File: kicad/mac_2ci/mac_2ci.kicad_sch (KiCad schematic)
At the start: 17 parts, among them U2 74HC00, U3 74HC00

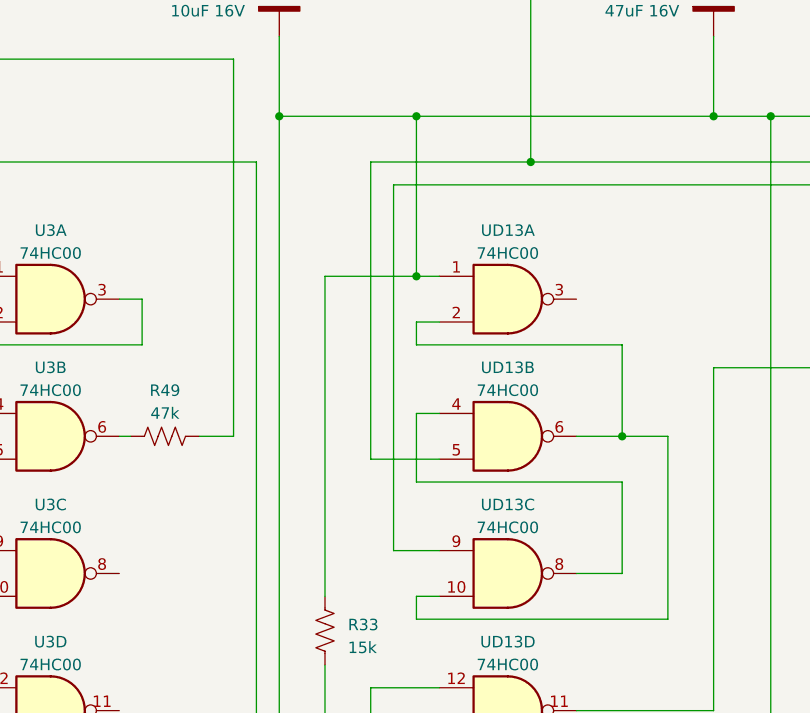
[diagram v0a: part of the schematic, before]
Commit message: Fix connections between UB-13 and UD-13
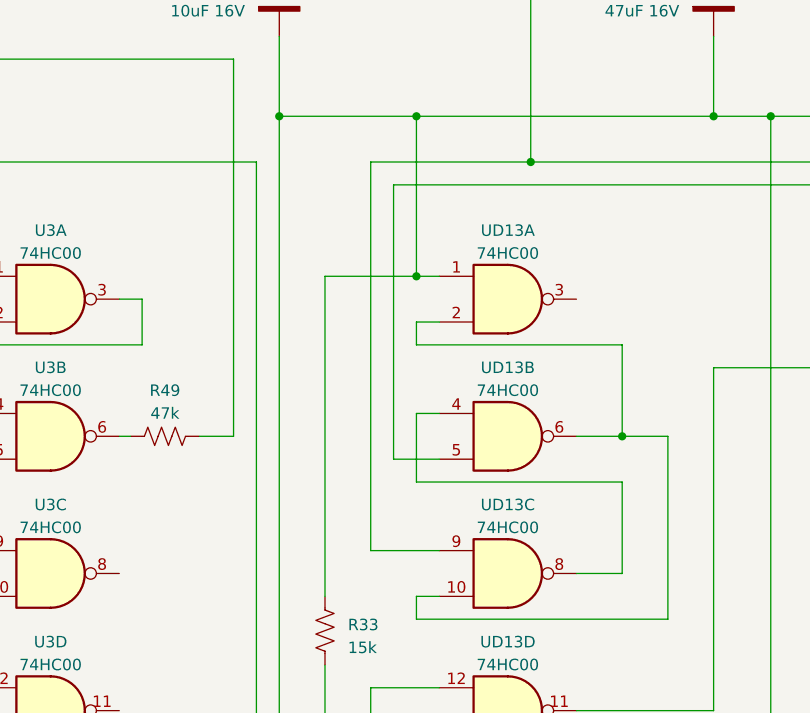
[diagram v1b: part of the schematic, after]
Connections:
- net at R27.1, UB13.4 (~{S}): now also UD13.5; no longer UD13.9
- net at C10.1, UB13.5 (Q): now also UD13.9; no longer UD13.5
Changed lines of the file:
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@@
-    (stroke (width 0) (type default))
-  )
-  (wire (pts (xy 135.89 93.98) (xy 143.51 93.98))
     (stroke (width 0) (type default))
   )
@@
     (stroke (width 0) (type default))
   )
+  (wire (pts (xy 135.89 104.14) (xy 143.51 104.14))
+    (stroke (width 0) (type default))
+  )
   (wire (pts (xy 110.49 76.2) (xy 110.49 81.28))
     (stroke (width 0) (type default))
@@
     (stroke (width 0) (type default))
   )
+  (wire (pts (xy 138.43 63.5) (xy 138.43 93.98))
+    (stroke (width 0) (type default))
+  )
   (wire (pts (xy 140.97 111.76) (xy 140.97 109.22))
     (stroke (width 0) (type default))
   )
-  (wire (pts (xy 138.43 104.14) (xy 143.51 104.14))
-    (stroke (width 0) (type default))
-  )
   (wire (pts (xy 143.51 78.74) (xy 140.97 78.74))
     (stroke (width 0) (type default))
@@
     (stroke (width 0) (type default))
   )
+  (wire (pts (xy 138.43 93.98) (xy 143.51 93.98))
+    (stroke (width 0) (type default))
+  )
   (wire (pts (xy 130.81 73.66) (xy 140.97 73.66))
     (stroke (width 0) (type default))
@@
     (stroke (width 0) (type default))
   )
-  (wire (pts (xy 138.43 63.5) (xy 138.43 104.14))
-    (stroke (width 0) (type default))
-  )
   (wire (pts (xy 173.99 36.83) (xy 173.99 39.37))
     (stroke (width 0) (type default))
@@
     (stroke (width 0) (type default))
   )
-  (wire (pts (xy 135.89 60.96) (xy 135.89 93.98))
+  (wire (pts (xy 135.89 60.96) (xy 135.89 104.14))
     (stroke (width 0) (type default))
   )
@@
     (pin "7")
     (instances
-      (project "trace_74hc"
+      (project "mac_2ci"
         (path "/8fd27ab9-1fd6-4fcb-9967-31c073270cfd"
           (reference "UB13") (unit 2)
@@
     (pin "7")
     (instances
-      (project "trace_74hc"
+      (project "mac_2ci"
         (path "/8fd27ab9-1fd6-4fcb-9967-31c073270cfd"
           (reference "UD13") (unit 3)
@@
     (pin "2")
     (instances
-      (project "trace_74hc"
+      (project "mac_2ci"
         (path "/8fd27ab9-1fd6-4fcb-9967-31c073270cfd"
           (reference "C13") (unit 1)
@@
     (pin "7")
     (instances
-      (project "trace_74hc"
+      (project "mac_2ci"
         (path "/8fd27ab9-1fd6-4fcb-9967-31c073270cfd"
           (reference "UD13") (unit 1)
@@
     (pin "2")
     (instances
-      (project "trace_74hc"
+      (project "mac_2ci"
         (path "/8fd27ab9-1fd6-4fcb-9967-31c073270cfd"
           (reference "R34") (unit 1)
@@
     (pin "2")
     (instances
-      (project "trace_74hc"
+      (project "mac_2ci"
         (path "/8fd27ab9-1fd6-4fcb-9967-31c073270cfd"
           (reference "R35") (unit 1)
@@
     (pin "7")
     (instances
-      (project "trace_74hc"
+      (project "mac_2ci"
         (path "/8fd27ab9-1fd6-4fcb-9967-31c073270cfd"
           (reference "UB13") (unit 1)
@@
     (pin "7")
     (instances
-      (project "trace_74hc"
+      (project "mac_2ci"
         (path "/8fd27ab9-1fd6-4fcb-9967-31c073270cfd"
           (reference "U3") (unit 5)
@@
     (pin "7")
     (instances
-      (project "trace_74hc"
+      (project "mac_2ci"
         (path "/8fd27ab9-1fd6-4fcb-9967-31c073270cfd"
           (reference "UD13") (unit 2)
@@
     (pin "7")
     (instances
-      (project "trace_74hc"
+      (project "mac_2ci"
         (path "/8fd27ab9-1fd6-4fcb-9967-31c073270cfd"
           (reference "U3") (unit 4)
@@
     (pin "2")
     (instances
-      (project "trace_74hc"
+      (project "mac_2ci"
         (path "/8fd27ab9-1fd6-4fcb-9967-31c073270cfd"
           (reference "R27") (unit 1)
@@
     (pin "7")
     (instances
-      (project "trace_74hc"
+      (project "mac_2ci"
         (path "/8fd27ab9-1fd6-4fcb-9967-31c073270cfd"
           (reference "UB13") (unit 3)
@@
     (pin "7")
     (instances
-      (project "trace_74hc"
+      (project "mac_2ci"
         (path "/8fd27ab9-1fd6-4fcb-9967-31c073270cfd"
           (reference "U3") (unit 1)
@@
     (pin "1")
     (instances
-      (project "trace_74hc"
+      (project "mac_2ci"
         (path "/8fd27ab9-1fd6-4fcb-9967-31c073270cfd"
           (reference "#PWR01") (unit 1)
@@
     (pin "2")
     (instances
-      (project "trace_74hc"
+      (project "mac_2ci"
         (path "/8fd27ab9-1fd6-4fcb-9967-31c073270cfd"
           (reference "R45") (unit 1)
@@
     (pin "7")
     (instances
-      (project "trace_74hc"
+      (project "mac_2ci"
         (path "/8fd27ab9-1fd6-4fcb-9967-31c073270cfd"
           (reference "U3") (unit 3)
@@
     (pin "7")
     (instances
-      (project "trace_74hc"
+      (project "mac_2ci"
         (path "/8fd27ab9-1fd6-4fcb-9967-31c073270cfd"
           (reference "U3") (unit 2)
@@
     (pin "2")
     (instances
-      (project "trace_74hc"
+      (project "mac_2ci"
         (path "/8fd27ab9-1fd6-4fcb-9967-31c073270cfd"
           (reference "R49") (unit 1)
@@
     (pin "2")
     (instances
-      (project "trace_74hc"
+      (project "mac_2ci"
         (path "/8fd27ab9-1fd6-4fcb-9967-31c073270cfd"
           (reference "R44") (unit 1)
@@
     (pin "2")
     (instances
-      (project "trace_74hc"
+      (project "mac_2ci"
         (path "/8fd27ab9-1fd6-4fcb-9967-31c073270cfd"
           (reference "C11") (unit 1)
@@
     (pin "2")
     (instances
-      (project "trace_74hc"
+      (project "mac_2ci"
         (path "/8fd27ab9-1fd6-4fcb-9967-31c073270cfd"
           (reference "C12") (unit 1)
@@
     (pin "2")
     (instances
-      (project "trace_74hc"
+      (project "mac_2ci"
         (path "/8fd27ab9-1fd6-4fcb-9967-31c073270cfd"
           (reference "C10") (unit 1)
@@
     (pin "2")
     (instances
-      (project "trace_74hc"
+      (project "mac_2ci"
         (path "/8fd27ab9-1fd6-4fcb-9967-31c073270cfd"
           (reference "C62") (unit 1)
@@
     (pin "2")
     (instances
-      (project "trace_74hc"
+      (project "mac_2ci"
         (path "/8fd27ab9-1fd6-4fcb-9967-31c073270cfd"
           (reference "R33") (unit 1)
@@
     (pin "2")
     (instances
-      (project "trace_74hc"
+      (project "mac_2ci"
         (path "/8fd27ab9-1fd6-4fcb-9967-31c073270cfd"
           (reference "C97") (unit 1)
@@
     (pin "7")
     (instances
-      (project "trace_74hc"
+      (project "mac_2ci"
         (path "/8fd27ab9-1fd6-4fcb-9967-31c073270cfd"
           (reference "U2") (unit 5)
@@
     (pin "7")
     (instances
-      (project "trace_74hc"
+      (project "mac_2ci"
         (path "/8fd27ab9-1fd6-4fcb-9967-31c073270cfd"
           (reference "UD13") (unit 4)

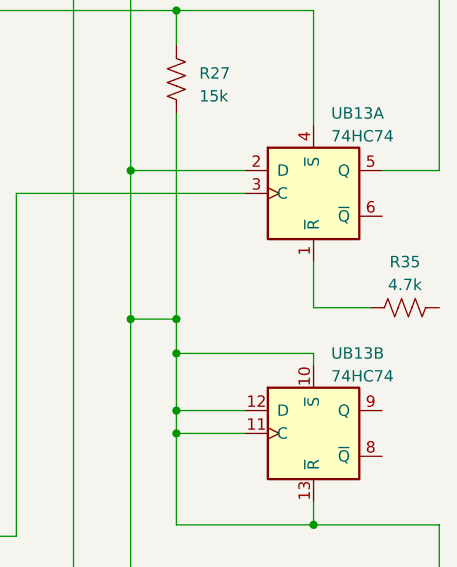
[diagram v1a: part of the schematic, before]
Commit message: Fix connection from UB-13 J1
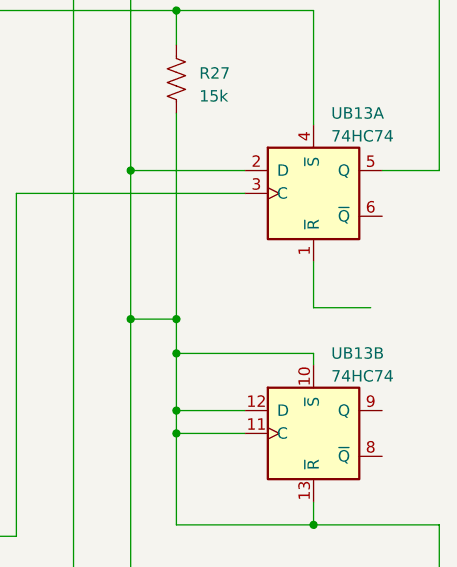
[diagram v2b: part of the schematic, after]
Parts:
- removed R35: 4.7k, symbol Device:R_US
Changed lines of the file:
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@@
-    )
-  )
-  (symbol (lib_id "Device:R_US") (at 217.17 96.52 90) (unit 1)
-    (in_bom yes) (on_board yes) (dnp no)
-    (property "Reference" "R35" (at 217.17 91.44 90)
-      (effects (font (size 1.27 1.27)))
-    )
-    (property "Value" "4.7k" (at 217.17 93.98 90)
-      (effects (font (size 1.27 1.27)))
-    )
-    (property "Footprint" "" (at 217.424 95.504 90)
-      (effects (font (size 1.27 1.27)) hide)
-    )
-    (property "Datasheet" "~" (at 217.17 96.52 0)
-      (effects (font (size 1.27 1.27)) hide)
-    )
-    (pin "1")
-    (pin "2")
-    (instances
-      (project "mac_2ci"
-        (path "/8fd27ab9-1fd6-4fcb-9967-31c073270cfd"
-          (reference "R35") (unit 1)
-        )
-      )
     )
   )

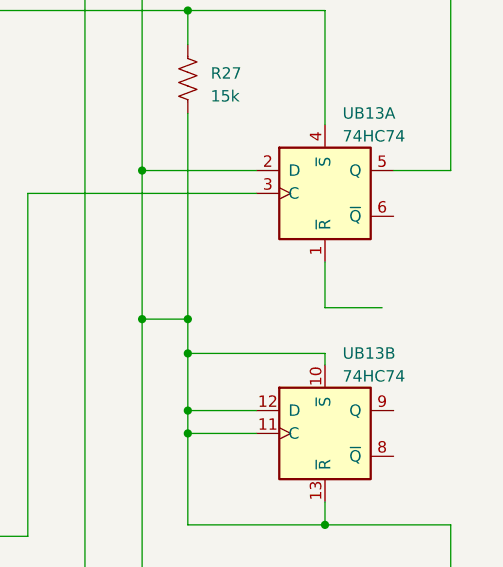
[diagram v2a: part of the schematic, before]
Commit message: Add connection UB13-1 to R112
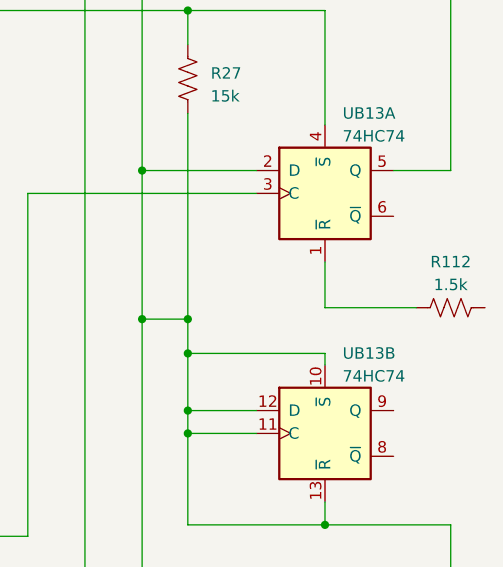
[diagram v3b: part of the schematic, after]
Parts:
- added R112: 1.5k, symbol Device:R_US
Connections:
- net at UB13.1 (~{R}): now also R112.1
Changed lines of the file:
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@@
     (stroke (width 0) (type default))
   )
-  (wire (pts (xy 207.01 96.52) (xy 213.36 96.52))
+  (wire (pts (xy 207.01 96.52) (xy 217.17 96.52))
     (stroke (width 0) (type default))
   )
@@
         )
       )
+    )
+  )
+  (symbol (lib_id "Device:R_US") (at 220.98 96.52 90) (unit 1)
+    (in_bom yes) (on_board yes) (dnp no)
+    (property "Reference" "R112" (at 220.98 91.44 90)
+      (effects (font (size 1.27 1.27)))
+    )
+    (property "Value" "1.5k" (at 220.98 93.98 90)
+      (effects (font (size 1.27 1.27)))
+    )
+    (property "Footprint" "" (at 221.234 95.504 90)
+      (effects (font (size 1.27 1.27)) hide)
+    )
+    (property "Datasheet" "~" (at 220.98 96.52 0)
+      (effects (font (size 1.27 1.27)) hide)
+    )
+    (pin "1")
+    (pin "2")
+    (instances
+      (project "mac_2ci"
+        (path "/8fd27ab9-1fd6-4fcb-9967-31c073270cfd"
+          (reference "R112") (unit 1)
+        )
+      )

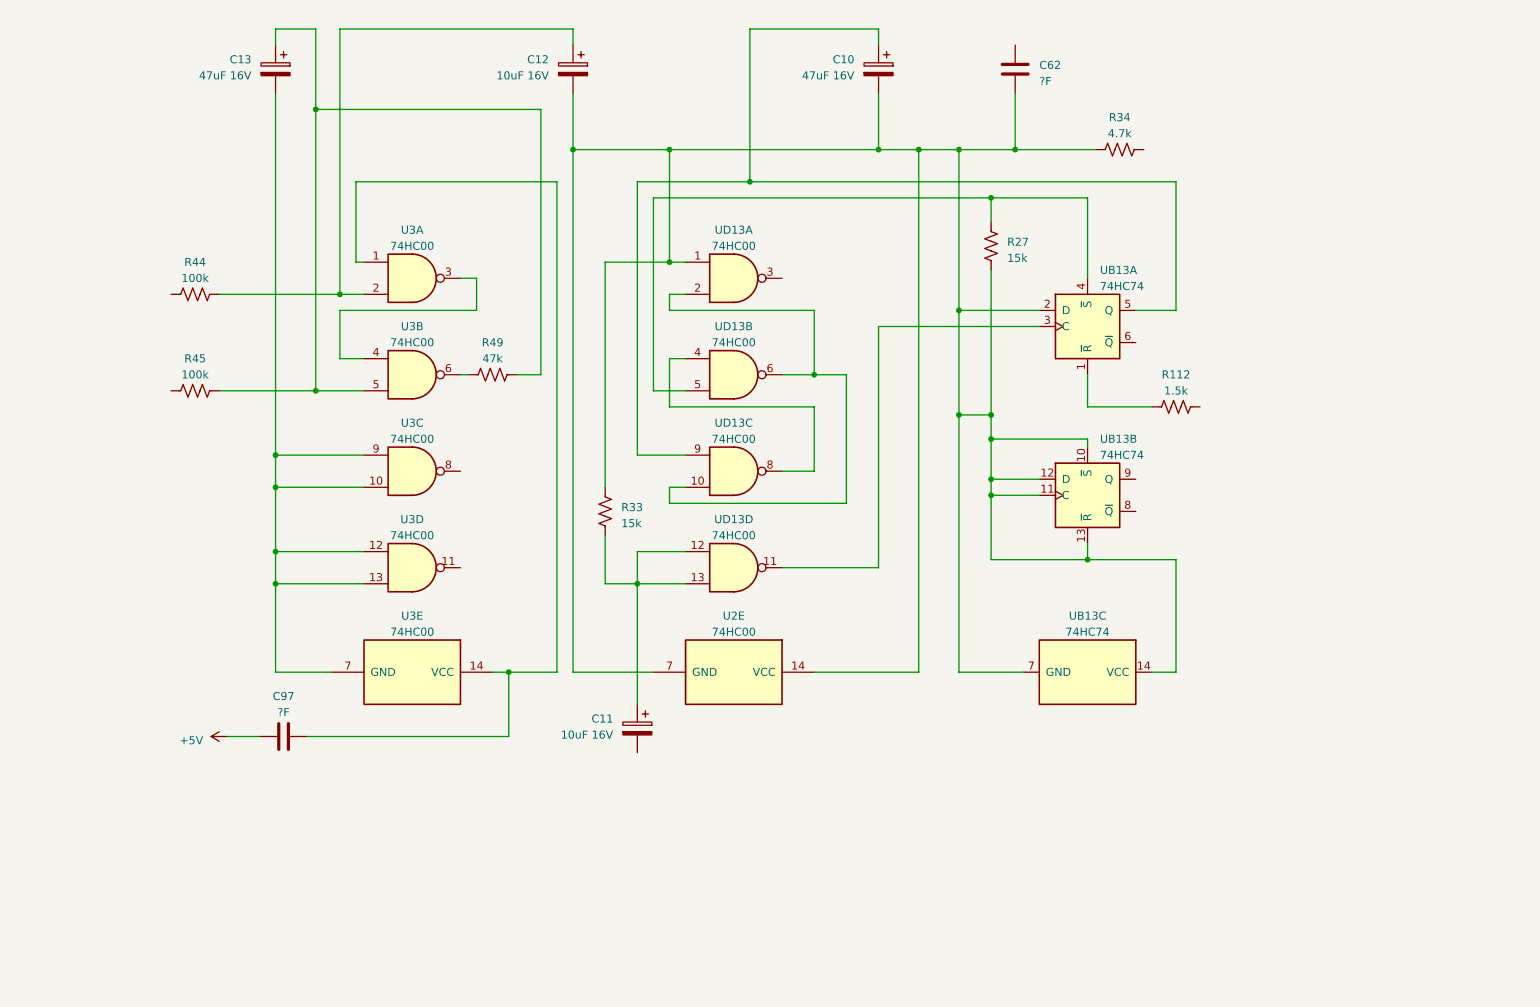
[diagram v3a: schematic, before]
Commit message: Fix mac_2ci schematic
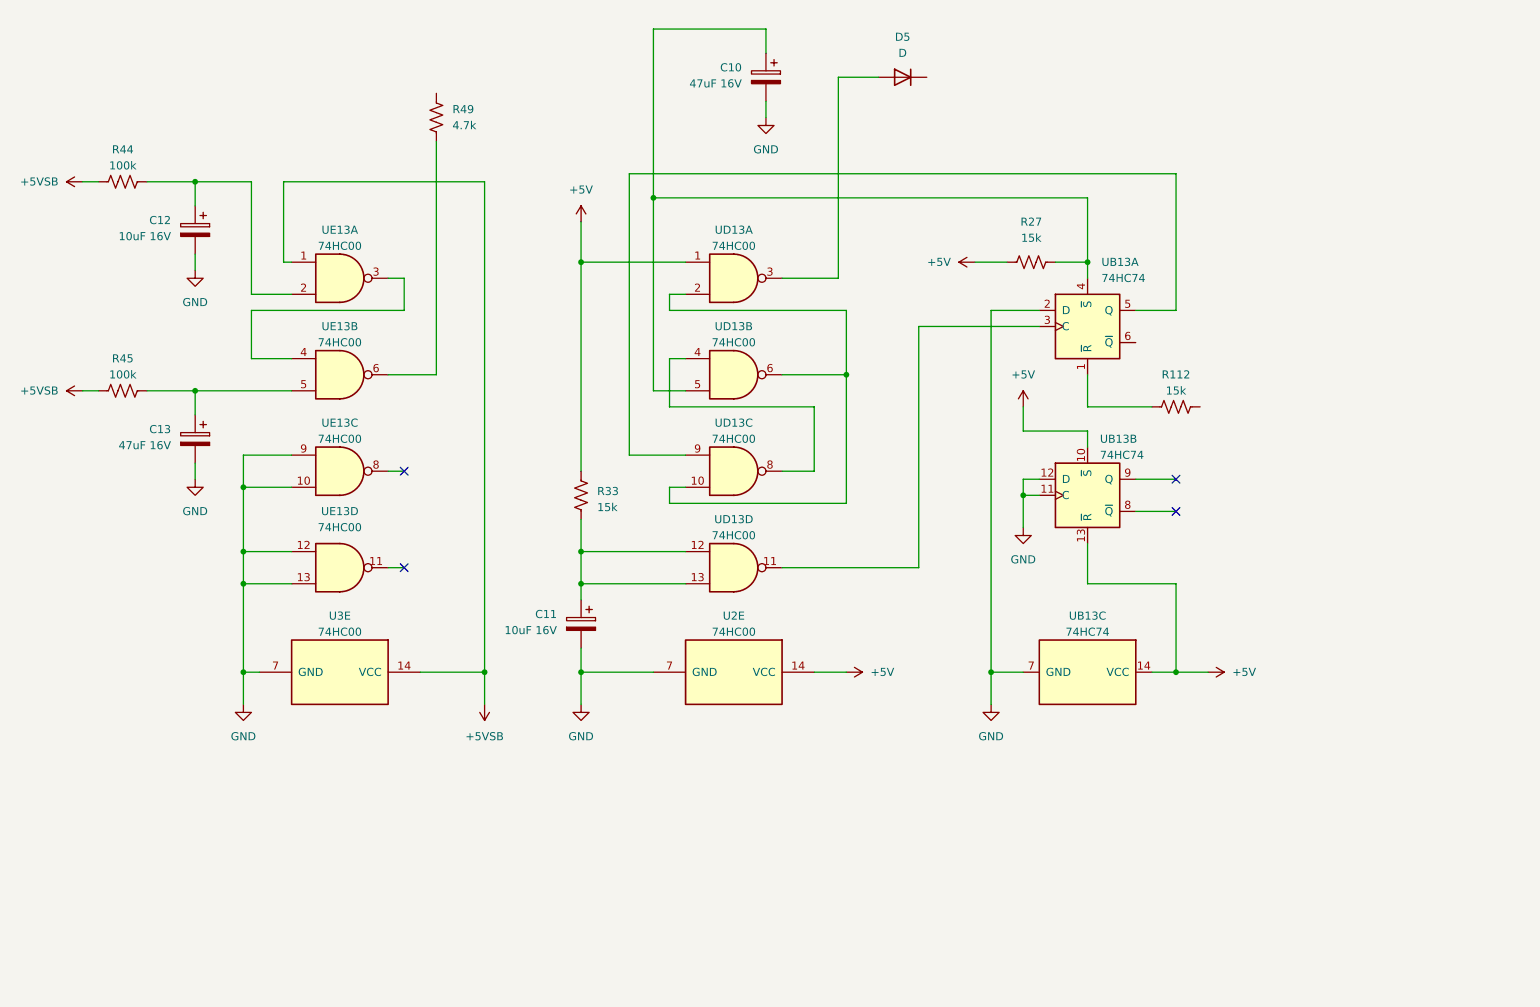
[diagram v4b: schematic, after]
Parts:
- removed C62, C97: ?F, symbol Device:C
- removed R34: 4.7k, symbol Device:R_US
- added D5: D, symbol Device:D
- R112: value 1.5k -> 15k
- R49: value 47k -> 4.7k
- renumbered U3 to UE13
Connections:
- net +5V: now also R27.2, R33.1, U2.14 (VCC), UB13.10 (~{S}), UB13.13 (~{R}), UB13.14 (VCC), UD13.1
- net GND: now reaches C10.2, C12.2, U2.7 (GND), UB13.11 (C), UB13.12 (D), UB13.2 (D), UB13.7 (GND)
- net GND: now also C11.2, C13.2, U3.7 (GND), UE13.10, UE13.12, UE13.13, UE13.9; no longer R27.2, R33.1, U2.14 (VCC), UB13.10 (~{S}), UB13.13 (~{R}), UB13.14 (VCC), UD13.1
- net at UB13.5 (Q), UD13.9: no longer C10.1
- net at C13.1, R45.2, UE13.5: no longer R49.2
- net at UD13.3: now also D5.2 (A)
- net at R27.1, UB13.4 (~{S}), UD13.5: now also C10.1
- net +5VSB: now reaches U3.14 (VCC), UE13.1
- net +5VSB: now also R44.1, R45.1
- net at UE13.6: now also R49.2; no longer R49.1
- no-connect marks 0 -> 4
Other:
- moved on the sheet: C10, C11, C12, C13, R27, R33, R44, R45, R49, U3E, UE13A, UE13B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
